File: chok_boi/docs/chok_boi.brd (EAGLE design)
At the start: 372 x 192 mm, 97 parts, among them U1 MPU-6000, U2 DRV8835

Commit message: Improve upper half board placement
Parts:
- removed C_REC_LD, C_REC_LF, C_REC_LH, C_REC_RD, C_REC_RF, C_REC_RH: 0.1uF, SparkFun:0603-CAP
- moved R_BOOT1 66.7 mm to (11.9, 3.78)
- moved R_B0 42.6 mm to (11.0, 10.2)
- moved C_E_H1 42.4 mm to (72.7, 49.2), turned to 270 degrees
- moved C_E_H2 42.0 mm to (74.8, 49.2), turned to 270 degrees
- moved U$13 34.0 mm to (58.0, 4.00), turned to 265 degrees
- moved SERIAL2 32.0 mm to (25.8, 36.0), turned to 90 degrees
- moved C_ERF2 31.4 mm to (54.9, 5.18)
- moved C_ERF1 31.2 mm to (54.9, 3.15)
- moved C_ELF1 30.7 mm to (55.1, 69.2), turned to 180 degrees
- moved C_ELF2 29.0 mm to (55.1, 71.2), turned to 180 degrees
- moved U$9 27.0 mm to (62.0, 10.0), turned to 267 degrees
- moved R_RLF 26.2 mm to (59.6, 64.4), turned to 90 degrees
- moved R_ELF 25.9 mm to (55.1, 66.6)
- moved R_RRF 25.7 mm to (59.3, 11.3)
- moved R_ERF_PD 25.6 mm to (49.9, 11.0), turned to 90 degrees
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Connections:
- net A3.3V: no longer C_REC_LD.1, C_REC_LF.1, C_REC_LH.1, C_REC_RD.1, C_REC_RF.1, C_REC_RH.1
- net AGND: no longer C_REC_LD.2, C_REC_LF.2, C_REC_LH.2, C_REC_RD.2, C_REC_RF.2, C_REC_RH.2
- net EM_D: now also U$5.PA7; no longer U$5.PA5
- net EM_H: now also U$5.PB0; no longer U$5.PA7
- net REC_RH: now also U$5.PA5; no longer U$5.PB0
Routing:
- net GND: track 203.2 -> 1.60 mm, vias 3 -> 0
- net H_EM: track 0.00 -> 34.0 mm
- net D2_EM: track 15.1 -> 0.00 mm
- net AGND: track 11.1 -> 0.00 mm
- net RF_EM: track 7.56 -> 0.00 mm
- net REC_RH: track 6.92 -> 0.00 mm
- net H2_EM: track 9.44 -> 3.63 mm
- net A3.3V: track 5.77 -> 0.00 mm
- net N$19: track 8.82 -> 3.22 mm
- net BOOT0: track 4.40 -> 0.00 mm
- net EM_H: track 3.67 -> 0.00 mm
- net D_EM: track 0.00 -> 3.65 mm
- net EM_RF: track 3.25 -> 0.00 mm
- net N$18: track 2.40 -> 0.00 mm
- net N$6: track 1.92 -> 0.00 mm
- removed copper zone on layer 1, net 3.3V
- removed copper zone on layer 1, net 5V

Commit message: Modify polygons to reduce routes. 79 airwires left
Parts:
- moved C_MB 272.5 mm to (15.9, 31.4)
- moved C_M2 272.3 mm to (15.6, 34.2)
- moved C_M1 269.0 mm to (19.1, 33.6), turned to 180 degrees
- moved C_VSS1 0.64 mm to (45.6, 30.8)
- moved R_ERF_PD 0.56 mm to (49.9, 11.6)
- moved C_VDD3 0.56 mm to (47.9, 30.9)
- moved C_VCAP1 0.30 mm to (62.2, 39.7)
- moved C_VDD2 0.28 mm to (48.3, 42.9)
- moved C_VDD1 0.18 mm to (60.0, 42.4)
- moved C_VCAP2 0.15 mm to (51.1, 44.9)
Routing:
- net GND: track 1.60 -> 174.2 mm, vias 0 -> 3
- net AGND: track 0.00 -> 74.9 mm
- net A3.3V: track 0.00 -> 69.2 mm, vias 0 -> 2
- net ENC_RA: track 0.00 -> 27.7 mm, vias 0 -> 2
- net EM_RF: track 0.00 -> 26.8 mm, vias 0 -> 2
- net EM_LF: track 0.00 -> 24.5 mm, vias 0 -> 4
- net ENC_RB: track 0.00 -> 23.7 mm, vias 0 -> 2
- net SCK: track 0.00 -> 17.6 mm, vias 0 -> 2
- net MOSI: track 0.00 -> 16.3 mm, vias 0 -> 2
- net 5V: track 82.8 -> 99.1 mm
- net TX: track 0.00 -> 16.0 mm, vias 0 -> 2
- net 3.3V: track 23.9 -> 38.0 mm
- net RX: track 0.00 -> 13.8 mm
- net RESET: track 0.00 -> 10.9 mm
- net RF_EM: track 0.00 -> 9.72 mm
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- added copper zone on layer 1, net 3.3V
- added copper zone on layer 1, net 5V

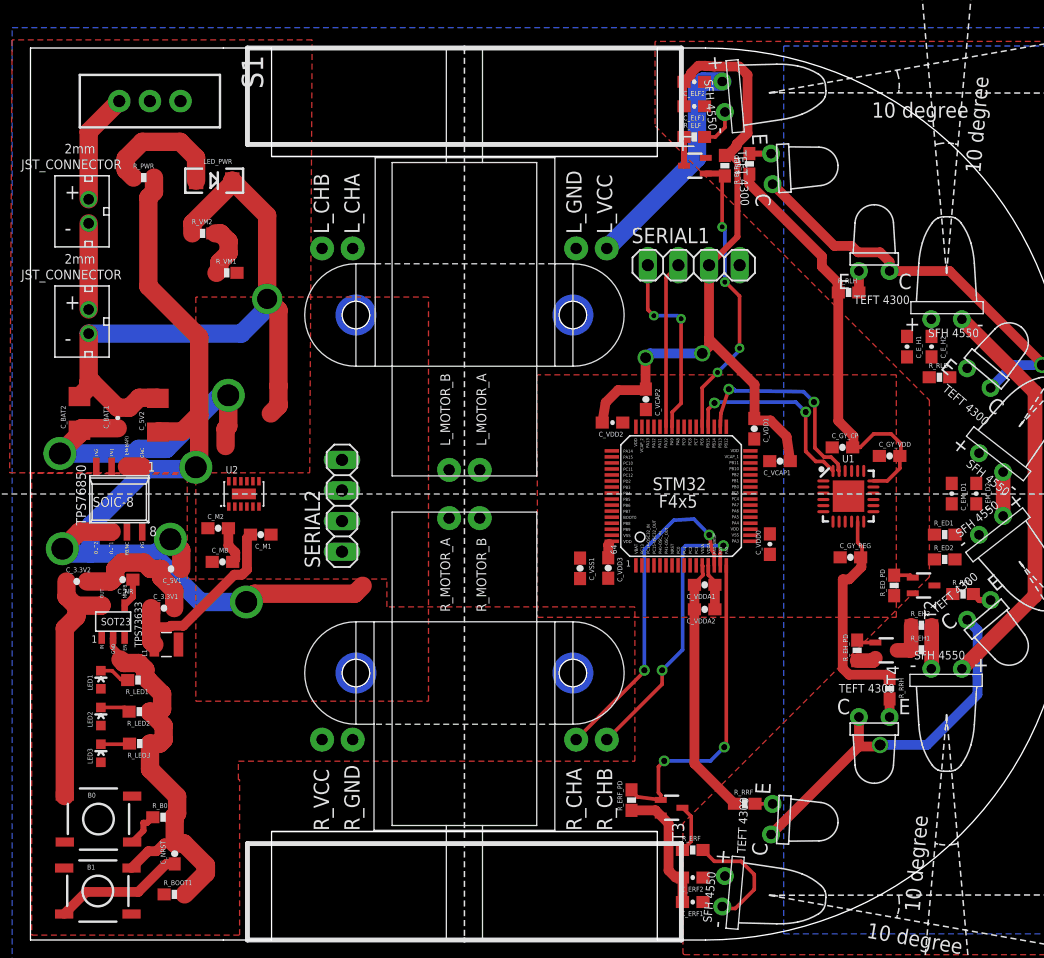
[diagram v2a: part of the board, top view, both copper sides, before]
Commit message: 74 airwires left
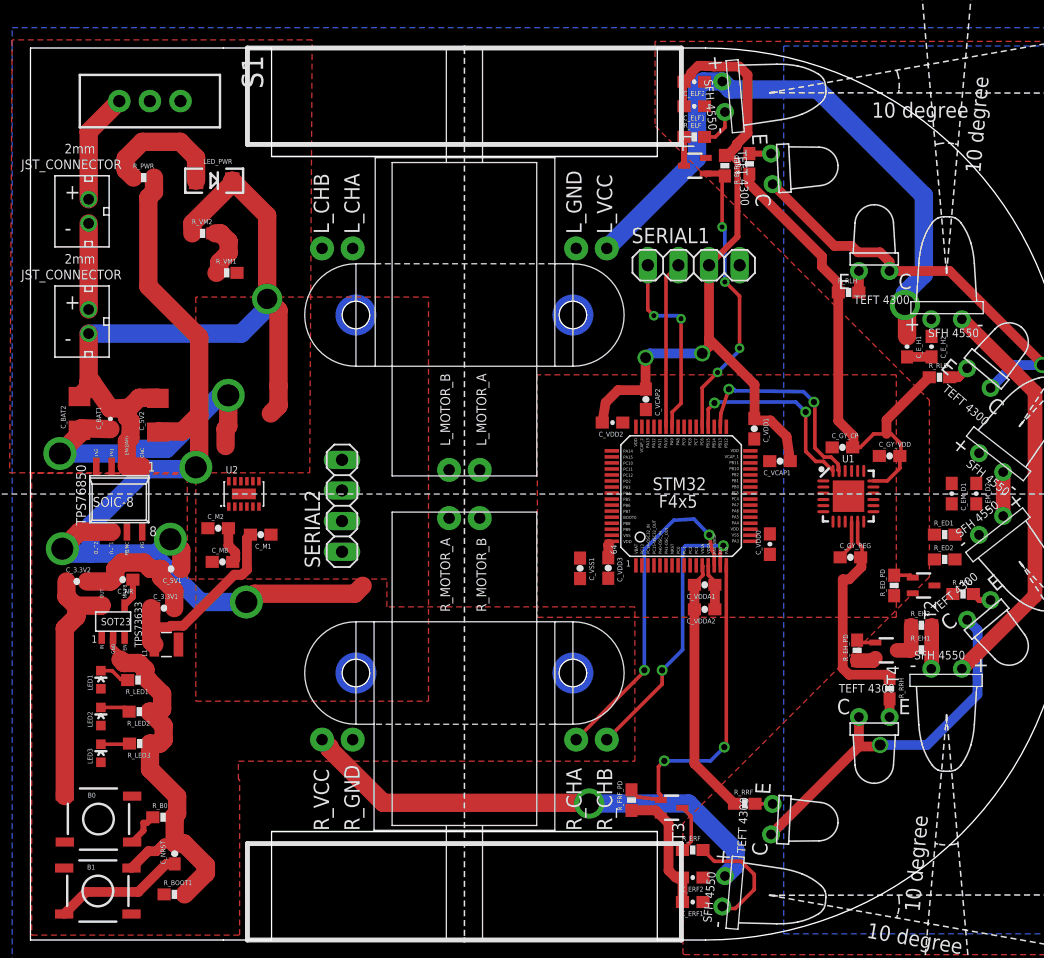
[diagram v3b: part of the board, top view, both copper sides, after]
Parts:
- moved C_BAT1 0.61 mm to (6.63, 43.2)
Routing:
- net 5V: track 99.1 -> 172.9 mm, vias 4 -> 6
- net GND: track 174.2 -> 181.7 mm
- net AGND: track 74.9 -> 81.0 mm
- net N$20: track 0.00 -> 3.35 mm
- net REC_LD: track 0.00 -> 1.75 mm
- net BATTERY: track 29.2 -> 28.6 mm
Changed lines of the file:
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@@
 <element name="C_GY_CP" library="SparkFun" package="0603-CAP" value="2.2nF" x="67.3608" y="40.8686"/>
 <element name="C_5V2" library="SparkFun-Passives" package="1206" value="100uF" x="10.5664" y="43.5356" rot="R90"/>
-<element name="C_BAT1" library="SparkFun-Capacitors" package="0603-CAP" value="0.1uF" x="7.239" y="43.307" rot="R90"/>
+<element name="C_BAT1" library="SparkFun-Capacitors" package="0603-CAP" value="0.1uF" x="6.6294" y="43.2308" rot="R90"/>
 <element name="C_BAT2" library="SparkFun-Passives" package="1206" value="100uF" x="4.064" y="43.688" rot="R90"/>
 <element name="C_ELF1" library="SparkFun-Capacitors" package="0603-CAP" value="4.7uF" x="55.0672" y="69.1642" rot="R180"/>
@@
 <wire x1="4.826" y1="45.85" x2="4.064" y2="45.088" width="1.524" layer="1"/>
 <wire x1="4.826" y1="46.3042" x2="5.0918" y2="46.3042" width="1.524" layer="1"/>
-<wire x1="5.0918" y1="46.3042" x2="7.239" y2="44.157" width="1.524" layer="1"/>
-<wire x1="7.239" y1="44.157" x2="8.1906" y2="44.157" width="1.524" layer="1"/>
-<wire x1="8.1906" y1="44.157" x2="9.017" y2="44.9834" width="1.524" layer="1"/>
-<wire x1="9.017" y1="44.9834" x2="10.5186" y2="44.9834" width="1.524" layer="1"/>
+<wire x1="5.0918" y1="46.3042" x2="6.6294" y2="44.0808" width="1.524" layer="1"/>
+<wire x1="8.1906" y1="44.157" x2="6.6294" y2="44.0808" width="1.524" layer="1"/>
+<wire x1="9.017" y1="44.9834" x2="8.1906" y2="44.157" width="1.524" layer="1"/>
+<wire x1="10.5186" y1="44.9834" x2="9.017" y2="44.9834" width="1.524" layer="1"/>
 <wire x1="10.5186" y1="44.9834" x2="10.5664" y2="44.9356" width="1.524" layer="1"/>
 <wire x1="4.826" y1="50.308" x2="17.4912" y2="50.308" width="1.524" layer="16"/>
@@
 <wire x1="10.4394" y1="7.366" x2="11.0862" y2="8.0128" width="0.8128" layer="1"/>
 <wire x1="11.0862" y1="8.0128" x2="11.9634" y2="8.0128" width="0.8128" layer="1"/>
-<wire x1="72.7202" y1="48.3752" x2="74.7522" y2="48.3752" width="0" layer="19" extent="1-1"/>
-<wire x1="62.7244" y1="41.7712" x2="72.7202" y2="48.3752" width="0" layer="19" extent="1-1"/>
-<wire x1="56.018" y1="64.8866" x2="57.6072" y2="65.0866" width="0" layer="19" extent="1-1"/>
-<wire x1="8.001" y1="39.276" x2="8.1906" y2="44.157" width="0" layer="19" extent="1-1"/>
+<wire x1="8.001" y1="39.276" x2="8.001" y2="41.36896875" width="1.524" layer="1"/>
+<wire x1="8.001" y1="41.36896875" x2="8.282884375" y2="41.63348125" width="1.524" layer="1"/>
+<wire x1="8.282884375" y1="41.63348125" x2="8.327025" y2="43.021565625" width="1.524" layer="1"/>
+<wire x1="8.327025" y1="43.021565625" x2="8.001" y2="43.369003125" width="1.524" layer="1"/>
+<wire x1="8.001" y1="43.369003125" x2="8.001" y2="43.9674" width="1.524" layer="1"/>
+<wire x1="8.001" y1="43.9674" x2="8.1906" y2="44.157" width="1.524" layer="1"/>
+<wire x1="72.7202" y1="48.3752" x2="74.7522" y2="48.3752" width="0.8128" layer="1"/>
+<wire x1="57.6072" y1="65.0866" x2="56.018" y2="64.8866" width="0" layer="19" extent="1-1"/>
 <wire x1="59.725" y1="33.58" x2="63.0292" y2="39.7256" width="0" layer="19" extent="1-1"/>
 <wire x1="61.341" y1="31.9922" x2="59.725" y2="33.58" width="0" layer="19" extent="1-1"/>
@@
 <wire x1="76.4286" y1="36.1832" x2="73.1918" y2="28.7632" width="0" layer="19" extent="1-1"/>
 <wire x1="78.4606" y1="36.1832" x2="76.4286" y2="36.1832" width="0" layer="19" extent="1-1"/>
+<wire x1="72.7202" y1="48.3752" x2="62.7244" y2="41.7712" width="0" layer="19" extent="1-1"/>
 <wire x1="49.8602" y1="10.7578" x2="47.9298" y2="30.011" width="0" layer="19" extent="1-1"/>
 <wire x1="52.2876" y1="10.3228" x2="52.138" y2="10.4724" width="0" layer="19" extent="1-1"/>
@@
 <vertex x="23.368" y="74.676"/>
 </polygon>
-<wire x1="7.239" y1="42.457" x2="4.233" y2="42.457" width="1.524" layer="1"/>
+<wire x1="6.6294" y1="42.3808" x2="4.233" y2="42.457" width="1.524" layer="1"/>
 <wire x1="4.233" y1="42.457" x2="4.064" y2="42.288" width="1.524" layer="1"/>
 <wire x1="4.064" y1="42.288" x2="4.064" y2="41.987" width="1.524" layer="1"/>
@@
 <wire x1="55.2958" y1="64.8608" x2="55.2958" y2="70.7136" width="1.524" layer="16"/>
 <wire x1="55.2958" y1="70.7136" x2="55.8037875" y2="71.2215875" width="1.524" layer="16"/>
-<wire x1="55.8037875" y1="71.2215875" x2="57.3912125" y2="71.2215875" width="1.524" layer="16"/>
-<wire x1="55.7902" y1="5.1816" x2="24.19" y2="16.625" width="0" layer="19" extent="1-1"/>
-<wire x1="55.2958" y1="64.8608" x2="72.7202" y2="50.0752" width="0" layer="19" extent="1-16"/>
+<wire x1="57.3912125" y1="71.2215875" x2="55.8037875" y2="71.2215875" width="1.524" layer="16"/>
+<wire x1="24.19" y1="16.625" x2="24.8156" y2="15.9994" width="1.524" layer="1"/>
+<wire x1="24.8156" y1="15.9994" x2="24.8156" y2="15.832025" width="1.524" layer="1"/>
+<wire x1="24.8156" y1="15.832025" x2="29.268425" y2="11.3792" width="1.524" layer="1"/>
+<wire x1="29.268425" y1="11.3792" x2="46.4058" y2="11.3792" width="1.524" layer="1"/>
+<wire x1="46.4058" y1="11.3792" x2="46.4058" y2="11.3741" width="1.524" layer="1"/>
+<wire x1="46.4058" y1="11.3741" x2="46.355" y2="11.3233" width="1.524" layer="1"/>
+<via x="46.355" y="11.3233" extent="1-16" drill="1.6764"/>
+<wire x1="46.355" y1="11.3233" x2="54.5897" y2="11.3233" width="1.524" layer="16"/>
+<wire x1="54.5897" y1="11.3233" x2="58.4962" y2="7.4168" width="1.524" layer="16"/>
+<wire x1="58.4962" y1="7.4168" x2="58.4962" y2="6.19235625" width="1.524" layer="16"/>
+<wire x1="58.4962" y1="6.19235625" x2="57.6125875" y2="5.30874375" width="1.524" layer="16"/>
+<wire x1="72.7202" y1="50.0752" x2="72.7202" y2="52.5018" width="1.524" layer="1"/>
+<wire x1="72.7202" y1="52.5018" x2="72.5424" y2="52.6796" width="1.524" layer="1"/>
+<via x="72.5424" y="52.6796" extent="1-16" drill="1.6764"/>
+<wire x1="72.5424" y1="52.6796" x2="72.5424" y2="53.6448" width="1.524" layer="16"/>
+<wire x1="72.5424" y1="53.6448" x2="74.1172" y2="55.2196" width="1.524" layer="16"/>
+<wire x1="74.1172" y1="55.2196" x2="74.1172" y2="61.753540625" width="1.524" layer="16"/>
+<wire x1="74.1172" y1="61.753540625" x2="65.31073125" y2="70.560009375" width="1.524" layer="16"/>
+<wire x1="65.31073125" y1="70.560009375" x2="58.052790625" y2="70.560009375" width="1.524" layer="16"/>
+<wire x1="58.052790625" y1="70.560009375" x2="57.3912125" y2="71.2215875" width="1.524" layer="16"/>
 </signal>
 <signal name="3.3V">
@@
 <contactref element="R_RLD" pad="2"/>
 <contactref element="U$5" pad="PC4"/>
-<wire x1="76.2626" y1="46.6852" x2="77.705728125" y2="47.433315625" width="0" layer="19" extent="1-1"/>
+<wire x1="76.2626" y1="46.6852" x2="76.9576125" y2="46.6852" width="0.8128" layer="1"/>
+<wire x1="76.9576125" y1="46.6852" x2="77.705728125" y2="47.433315625" width="0.8128" layer="1"/>
 <wire x1="59.725" y1="36.58" x2="76.2626" y2="46.6852" width="0" layer="19" extent="1-1"/>
 </signal>
@@
 <wire x1="68.2108" y1="40.8686" x2="68.834" y2="40.8686" width="0.3048" layer="1"/>
 <wire x1="68.834" y1="40.8686" x2="69.9516" y2="41.9862" width="0.3048" layer="1"/>
-<wire x1="69.9516" y1="41.9862" x2="71.3994" y2="41.9862" width="0.3048" layer="1"/>
+<wire x1="71.0184" y1="41.9862" x2="69.9516" y2="41.9862" width="0.3048" layer="1"/>
+<wire x1="71.0184" y1="41.9862" x2="71.3994" y2="41.9862" width="0.3048" layer="1"/>
 <wire x1="71.3994" y1="41.9862" x2="72.2122" y2="41.1734" width="0.3048" layer="1"/>
 <wire x1="72.2122" y1="41.1734" x2="72.2122" y2="40.2472" width="0.3048" layer="1"/>
 <wire x1="72.2122" y1="40.2472" x2="72.1224" y2="40.1574" width="0.3048" layer="1"/>
-<wire x1="71.3994" y1="41.9862" x2="74.5626" y2="46.6852" width="0" layer="19" extent="1-1"/>
-<wire x1="68.623" y1="34.7084" x2="69.9296" y2="38.0867" width="0" layer="19" extent="1-1"/>
+<wire x1="74.5626" y1="46.6852" x2="71.0184" y2="43.141" width="0.8128" layer="1"/>
+<wire x1="71.0184" y1="43.141" x2="71.0184" y2="41.9862" width="0.8128" layer="1"/>
+<wire x1="68.9356" y1="30.9372" x2="76.5184" y2="28.702" width="0" layer="19" extent="1-1"/>
+<wire x1="69.9296" y1="38.0867" x2="68.623" y2="34.7084" width="0" layer="19" extent="1-1"/>
 <wire x1="65.7772" y1="38.0867" x2="68.2108" y2="40.8686" width="0" layer="19" extent="1-1"/>
-<wire x1="76.5184" y1="28.702" x2="68.9356" y2="30.9372" width="0" layer="19" extent="1-1"/>
 <wire x1="55.7784" y1="30.34555" x2="67.3862" y2="29.9212" width="0" layer="19" extent="1-1"/>
 <wire x1="20.574" y1="45.974" x2="55.725" y2="31.08" width="0" layer="19" extent="1-1"/>
@@
 <contactref element="C_GY_REG" pad="1"/>
 <contactref element="U1" pad="10"/>
-<wire x1="67.1712" y1="31.75" x2="68.1209" y2="34.7084" width="0" layer="19" extent="1-1"/>
+<wire x1="67.1712" y1="31.75" x2="68.1209" y2="32.6997" width="0.3048" layer="1"/>
+<wire x1="68.1209" y1="32.6997" x2="68.1209" y2="34.7084" width="0.3048" layer="1"/>
 </signal>
 <signal name="N$22">

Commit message: In middle of reworking traces
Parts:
- R_BOOT1: device SparkFun-Passives:0603-RES -> SparkFun-Passives:0402-RES
- moved LED1 91.7 mm to (97.5, 19.9), turned to 270 degrees
- moved LED2 91.7 mm to (97.5, 16.9), turned to 270 degrees
- moved LED3 91.7 mm to (97.5, 13.8), turned to 270 degrees
- moved R_LED2 91.7 mm to (100.7, 17.3)
- moved R_LED1 91.7 mm to (100.6, 19.9)
- moved R_LED3 91.7 mm to (100.8, 14.6)
- moved R_BOOT1 61.0 mm to (61.8, 38.9)
- moved L1 44.5 mm to (55.8, 23.2)
- moved SERIAL2 38.3 mm to (61.5, 50.1)
- moved LED_PWR 13.3 mm to (18.2, 50.0)
- moved R_PWR 13.3 mm to (12.4, 50.2)
- moved U$1 12.4 mm to (7.32, 63.4), turned to 270 degrees
- moved C_MB 11.4 mm to (20.1, 42.0), turned to 180 degrees
- moved U$2 9.48 mm to (13.8, 63.4), turned to 270 degrees
- moved C_3.3V2 8.85 mm to (7.21, 21.6), turned to 180 degrees
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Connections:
- net EM_H: now also U$5.PA6; no longer U$5.PB0
- net REC_LD: now also U$5.PC5; no longer U$5.PC4
- net REC_LF: now also U$5.PB1; no longer U$5.PC5
- net REC_LH: now also U$5.PB0; no longer U$5.PB1
- net REC_RD: now also U$5.PC4; no longer U$5.PA6
- net SS1: now also U$5.PC7; no longer U$5.PC8
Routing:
- net 5V: track 172.9 -> 9.46 mm, vias 6 -> 0
- net GND: track 181.7 -> 31.9 mm, vias 3 -> 15
- net AGND: track 81.0 -> 36.5 mm, vias 0 -> 12
- net REC_LF: track 1.80 -> 36.4 mm
- net A3.3V: track 69.2 -> 103.3 mm, vias 2 -> 0
- net BATTERY: track 28.6 -> 0.00 mm, vias 2 -> 0
- net ENC_RA: track 27.7 -> 0.00 mm, vias 2 -> 0
- net EM_RF: track 26.8 -> 0.00 mm, vias 2 -> 0
- net REC_RF: track 1.46 -> 28.0 mm
- net REC_RH: track 1.50 -> 26.5 mm
- net REC_LD: track 1.75 -> 26.1 mm, vias 0 -> 2
- net REC_RD: track 1.64 -> 25.8 mm, vias 0 -> 2
- net ENC_RB: track 23.7 -> 0.00 mm, vias 2 -> 0
- net EM_LF: track 24.5 -> 1.62 mm, vias 4 -> 0
- net REC_LH: track 1.78 -> 23.9 mm
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- added copper zone on layer 1, net AGND
- added copper zone on layer 1, net GND
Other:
- outline, holes or cut-outs redrawn

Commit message: More routing
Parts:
- added C1: (no value), SparkFun:1210
- C_5V2, C_BAT2: value 100uF -> 47uF; device SparkFun-Passives:1206 -> SparkFun:1210
- C_MB: device SparkFun:0603-CAP -> Volks73-Kemet:X
- moved LED1 101.5 mm to (3.28, 57.6)
- moved LED2 101.5 mm to (3.28, 54.6)
- moved LED3 101.5 mm to (3.28, 51.5)
- moved R_LED1 101.5 mm to (6.35, 57.6)
- moved R_LED2 101.5 mm to (6.46, 55.0)
- moved R_LED3 101.5 mm to (6.50, 52.3)
- moved C_5V2 12.9 mm to (3.28, 32.9), turned to 270 degrees
- moved U$16 7.69 mm to (18.9, 52.0)
- moved U$15 7.56 mm to (18.2, 53.1)
- moved SERIAL2 4.69 mm to (56.8, 49.6), turned to 0 degrees
- moved C_BAT2 4.18 mm to (7.57, 43.9), turned to 0 degrees
- moved SERIAL1 3.34 mm to (56.8, 53.2)
- moved C_MB 2.02 mm to (21.7, 43.3), turned to 0 degrees
- moved C_VCAP2 0.87 mm to (50.4, 45.4)
- moved C_M2 0.45 mm to (20.5, 39.1)
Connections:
- net BATTERY: now also C_MB.A; no longer C_MB.2
- net EM_LF: now also U$5.PA11; no longer U$5.PC6
- net LED1: now also U$5.PC6; no longer U$5.PA11
- net MGND: now also C_MB.C; no longer C_MB.1
- net PWMLB: now also U$5.PB6; no longer U$5.PB7
- net PWMLF: now also U$5.PB7; no longer U$5.PB6
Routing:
- net RESET: track 0.00 -> 75.1 mm, vias 0 -> 4
- net ENC_LB: track 0.00 -> 32.2 mm
- net ENC_LA: track 0.00 -> 28.7 mm
- net ENC_RA: track 0.00 -> 22.3 mm, vias 0 -> 1
- net ENC_RB: track 0.00 -> 22.2 mm, vias 0 -> 1
- net EM_LF: track 1.62 -> 21.6 mm
- net EM_RF: track 0.00 -> 19.5 mm, vias 0 -> 2
- net A3.3V: track 103.3 -> 121.3 mm
- net 3.3V: track 17.9 -> 33.8 mm
- net TX: track 0.00 -> 15.1 mm
- net SWCLK: track 0.00 -> 15.0 mm, vias 0 -> 2
- net RX: track 0.00 -> 12.8 mm
- net SWDIO: track 0.00 -> 12.3 mm, vias 0 -> 2
- net GND: track 31.9 -> 36.9 mm, vias 15 -> 16
- net BOOT0: track 0.00 -> 3.15 mm
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
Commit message: Move LEDs on MCU and route more. 22 airwires left
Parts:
- removed C1: (no value), SparkFun:1210
- moved U$15 2.04 mm to (20.2, 53.4)
- moved R_VM1 1.49 mm to (17.3, 56.4)
- moved U$16 0.45 mm to (19.3, 52.3)
- moved B0 0.44 mm to (5.11, 8.00)
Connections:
- net LED1: now also U$5.PC10; no longer U$5.PC6
- net LED2: now also U$5.PC11; no longer U$5.PC10
- net LED3: now also U$5.PC12; no longer U$5.PC0
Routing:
- net GND: track 36.9 -> 123.9 mm, vias 16 -> 20
- net VOLTMETER: track 0.00 -> 60.1 mm, vias 0 -> 2
- net AGND: track 36.5 -> 91.4 mm, vias 12 -> 14
- net PWMRF: track 0.00 -> 37.1 mm
- net PWMRB: track 0.00 -> 36.3 mm
- net PWMLF: track 0.00 -> 35.7 mm
- net PWMLB: track 0.00 -> 34.6 mm
- net 5V: track 9.46 -> 31.8 mm, vias 0 -> 2
- net N$8: track 0.00 -> 6.35 mm
- net BOOT0: track 3.15 -> 5.49 mm
- net N$21: track 0.00 -> 1.96 mm
- net N$16: track 0.00 -> 1.75 mm
- net N$12: track 0.00 -> 1.48 mm
